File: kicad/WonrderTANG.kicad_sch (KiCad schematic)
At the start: 31 parts, among them CON1 MSX-CONNECTOR, J1 Conn_02x01, J2 AudioJack3, J3 Conn_02x01, Q1 2N3904, U1 SN74LVC245AN, U2 SN74LVC245AN, U3 SN74LVC245AN, U4 SN74LVC245AN, U5 Tang_Nano_20k, U6 SN74LVC245AN

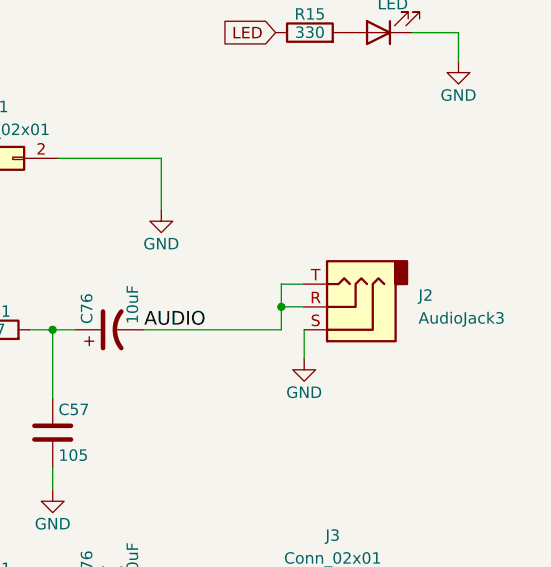
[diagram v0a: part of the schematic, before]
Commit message: [kicad] Use alternate audio connector SJ1-3525N
Exchange the SJ1-3533NG mono audio connector with the more common
(at least in Europe and some large asian shops) SJ1-3525N stereo
connector, keeping the same orientation.
To fit the new connector the board led is slightly moved too.

Signed-off-by: Albert Herranz <albert_herranz@yahoo.es>
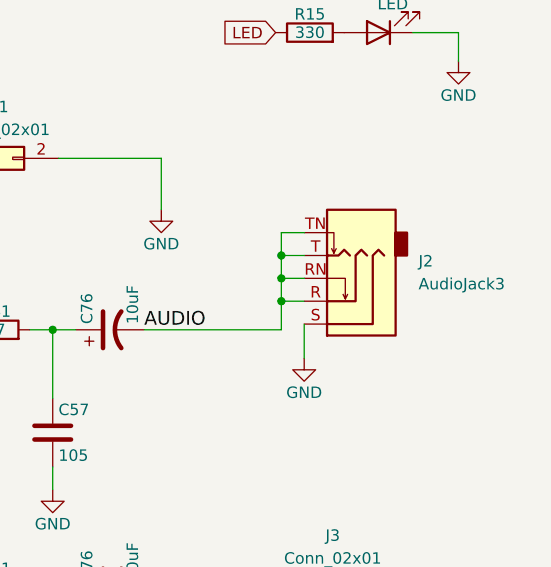
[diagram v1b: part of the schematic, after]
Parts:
- J2: footprint Connector_Audio:Jack_3.5mm_CUI_SJ1-3533NG_Horizontal -> Connector_Audio:Jack_3.5mm_CUI_SJ1-3525N_Horizontal; symbol Connector_Audio:AudioJack3 -> Connector_Audio:AudioJack3_SwitchTR
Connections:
- net AUDIO: now also J2.RN, J2.TN
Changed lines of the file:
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@@
     (date "2023-03-01")
   )
+  (junction (at 363.22 106.68) (diameter 0) (color 0 0 0 0)
+  )
+  (junction (at 363.22 101.6) (diameter 0) (color 0 0 0 0)
+  )
+  (junction (at 363.22 104.14) (diameter 0) (color 0 0 0 0)
+  )
   (junction (at 101.6 147.32) (diameter 0) (color 0 0 0 0)
   )
@@
   )
   (junction (at 101.6 154.94) (diameter 0) (color 0 0 0 0)
-  )
-  (junction (at 363.22 107.315) (diameter 0) (color 0 0 0 0)
   )
   (junction (at 337.82 138.43) (diameter 0) (color 0 0 0 0)
@@
     (stroke (width 0) (type default))
   )
-  (wire (pts (xy 365.76 109.855) (xy 365.76 113.03))
+  (wire (pts (xy 365.76 109.22) (xy 365.76 113.03))
     (stroke (width 0) (type default))
   )
@@
     (stroke (width 0) (type default))
   )
-  (wire (pts (xy 363.22 104.775) (xy 363.22 107.315))
+  (wire (pts (xy 363.22 104.14) (xy 363.22 106.68))
     (stroke (width 0) (type default))
   )
@@
     (stroke (width 0) (type default))
   )
-  (wire (pts (xy 363.22 107.315) (xy 365.76 107.315))
+  (wire (pts (xy 363.22 106.68) (xy 365.76 106.68))
     (stroke (width 0) (type default))
   )
@@
     (stroke (width 0) (type default))
   )
+  (wire (pts (xy 363.22 99.06) (xy 363.22 101.6))
+    (stroke (width 0) (type default))
+  )
   (wire (pts (xy 295.91 63.5) (xy 299.72 63.5))
     (stroke (width 0) (type default))
@@
     (stroke (width 0) (type default))
   )
+  (wire (pts (xy 365.76 99.06) (xy 363.22 99.06))
+    (stroke (width 0) (type default))
+  )
   (wire (pts (xy 149.86 99.06) (xy 152.4 99.06))
     (stroke (width 0) (type default))
@@
     (stroke (width 0) (type default))
   )
+  (wire (pts (xy 365.76 101.6) (xy 363.22 101.6))
+    (stroke (width 0) (type default))
+  )
   (wire (pts (xy 101.6 147.32) (xy 101.6 149.86))
     (stroke (width 0) (type default))
@@
     (stroke (width 0) (type default))
   )
-  (wire (pts (xy 365.76 104.775) (xy 363.22 104.775))
+  (wire (pts (xy 365.76 104.14) (xy 363.22 104.14))
     (stroke (width 0) (type default))
   )
@@
     (stroke (width 0) (type default))
   )
-  (wire (pts (xy 363.22 109.855) (xy 363.22 107.315))
-    (stroke (width 0) (type default))
-  )
   (wire (pts (xy 149.86 139.7) (xy 152.4 139.7))
     (stroke (width 0) (type default))
@@
     (stroke (width 0) (type default))
   )
+  (wire (pts (xy 363.22 106.68) (xy 363.22 109.855))
+    (stroke (width 0) (type default))
+  )
   (wire (pts (xy 101.6 114.3) (xy 104.14 114.3))
     (stroke (width 0) (type default))
@@
   )
   (wire (pts (xy 149.86 152.4) (xy 152.4 152.4))
+    (stroke (width 0) (type default))
+  )
+  (wire (pts (xy 363.22 101.6) (xy 363.22 104.14))
     (stroke (width 0) (type default))
   )
@@
     )
   )
-  (symbol (lib_id "Connector_Audio:AudioJack3") (at 370.84 107.315 180) (unit 1)
+  (symbol (lib_id "Connector_Audio:AudioJack3_SwitchTR") (at 370.84 106.68 180) (unit 1)
     (in_bom yes) (on_board yes) (dnp no) (fields_autoplaced)
-    (property "Reference" "J2" (at 378.46 106.045 0)
+    (property "Reference" "J2" (at 378.46 102.235 0)
       (effects (font (size 1.27 1.27)) (justify right))
     )
-    (property "Value" "AudioJack3" (at 378.46 108.585 0)
+    (property "Value" "AudioJack3" (at 378.46 104.775 0)
       (effects (font (size 1.27 1.27)) (justify right))
     )
-    (property "Footprint" "Connector_Audio:Jack_3.5mm_CUI_SJ1-3533NG_Horizontal" (at 370.84 107.315 0)
-      (effects (font (size 1.27 1.27)) hide)
-    )
-    (property "Datasheet" "~" (at 370.84 107.315 0)
+    (property "Footprint" "Connector_Audio:Jack_3.5mm_CUI_SJ1-3525N_Horizontal" (at 370.84 106.68 0)
+      (effects (font (size 1.27 1.27)) hide)
+    )
+    (property "Datasheet" "~" (at 370.84 106.68 0)
       (effects (font (size 1.27 1.27)) hide)
     )
     (pin "R")
+    (pin "RN")
     (pin "S")
     (pin "T")
+    (pin "TN")
     (instances
       (project "WonrderTANG"
